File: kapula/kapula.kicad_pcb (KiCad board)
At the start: 4 copper layers, 50 x 59 mm, 167 parts, among them J1 Conn_02x10_Odd_Even, J12 U.FL, J13 U.FL, J3 Conn_02x10_Odd_Even, J4 Conn_ARM_JTAG_SWD_10, J5 U.FL, J9 U.FL, Q1 AO3401A, Q2 AO3401A, Q3 AO3400A, Q4 BSS84, Q5 AO3400A, Q6 AO3400A, T1 BW21S7511A01TF, T2 BW21S7511A01TF, T3 BW21S7511A01TF, T4 BW21S7511A01TF, U1 XC6206P332MR, U2 TP4054, U3 DW01+G, U5 EFR32FG14P233F256GM48-B, U6 XA213-G4J, X1 DSB221SDN, Y1 32768 Hz

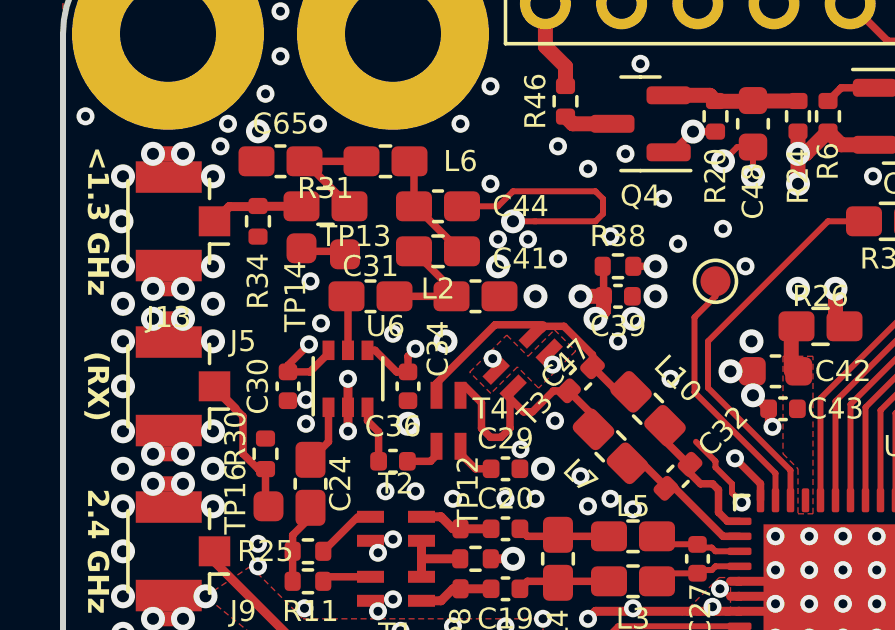
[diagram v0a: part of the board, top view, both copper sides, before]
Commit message: PCB: Improve RF layout
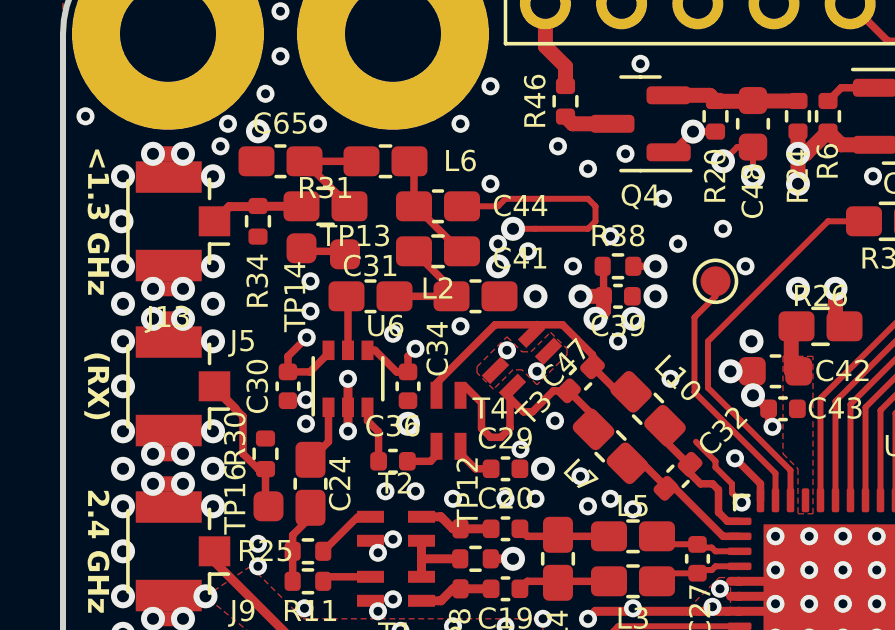
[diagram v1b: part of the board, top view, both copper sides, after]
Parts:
- moved NT2 0.25 mm to (115.5, 67.5)
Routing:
- net Net-(C44-Pad2): track 7.91 -> 7.31 mm

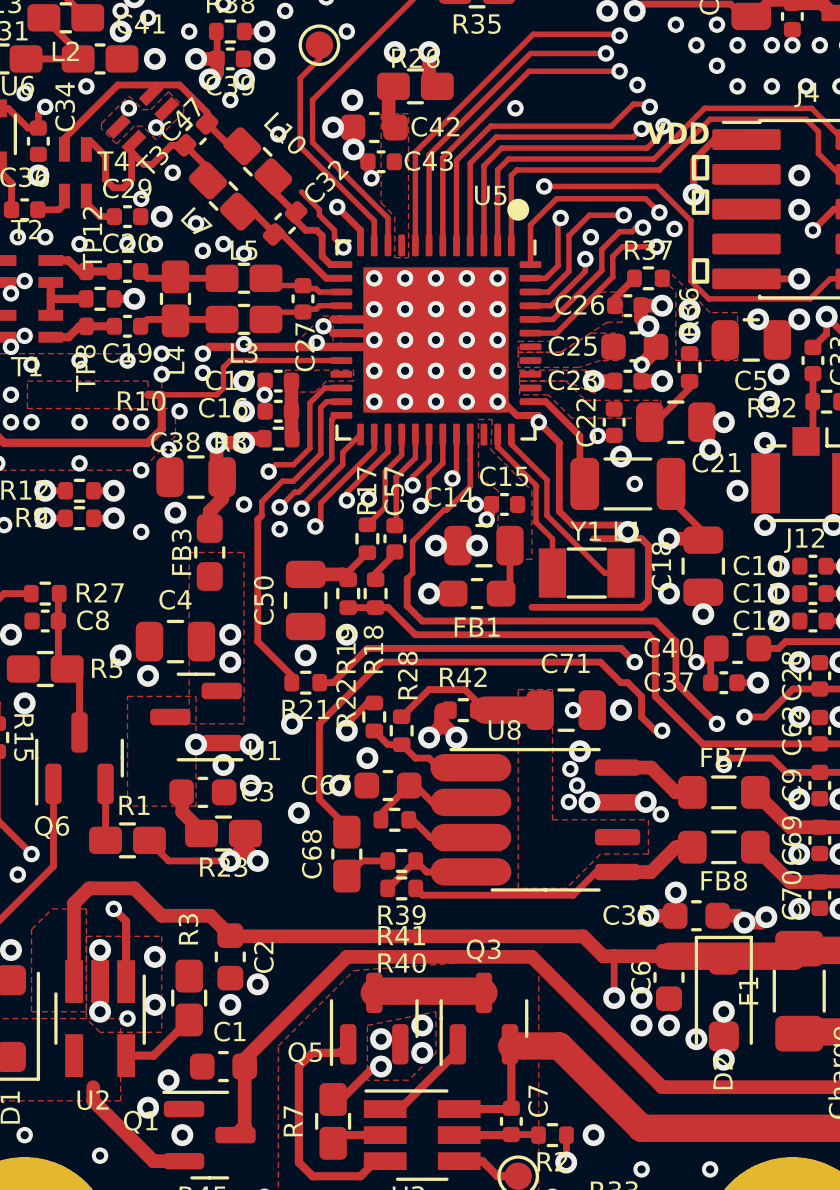
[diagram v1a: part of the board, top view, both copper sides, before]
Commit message: PCB: Make some planes and fills more continuous
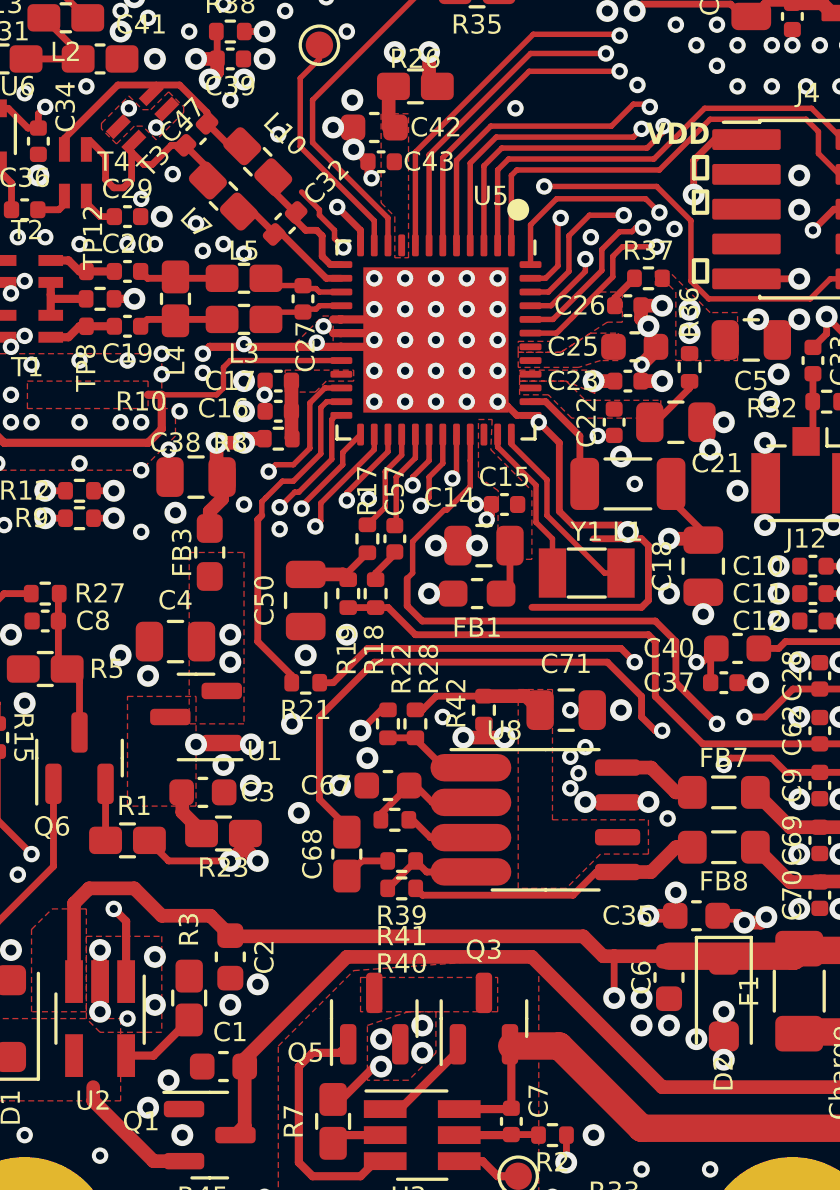
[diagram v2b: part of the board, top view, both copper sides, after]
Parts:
- moved R42 0.75 mm to (127.8, 93.5), turned to 90 degrees
- moved R22 0.56 mm to (124.2, 94.0)
- moved R28 0.56 mm to (125.2, 94.0)
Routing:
- net /BP_MID: track 4.05 -> 0.00 mm
- net GND: track 72.3 -> 71.3 mm, vias 388 -> 389
- net /VBAT: track 10.1 -> 9.17 mm
- net /AMP_VDD: track 5.77 -> 4.97 mm
- net /SPK_SDN: track 61.3 -> 60.6 mm
- added copper zone on F.Cu, net /BP_MID

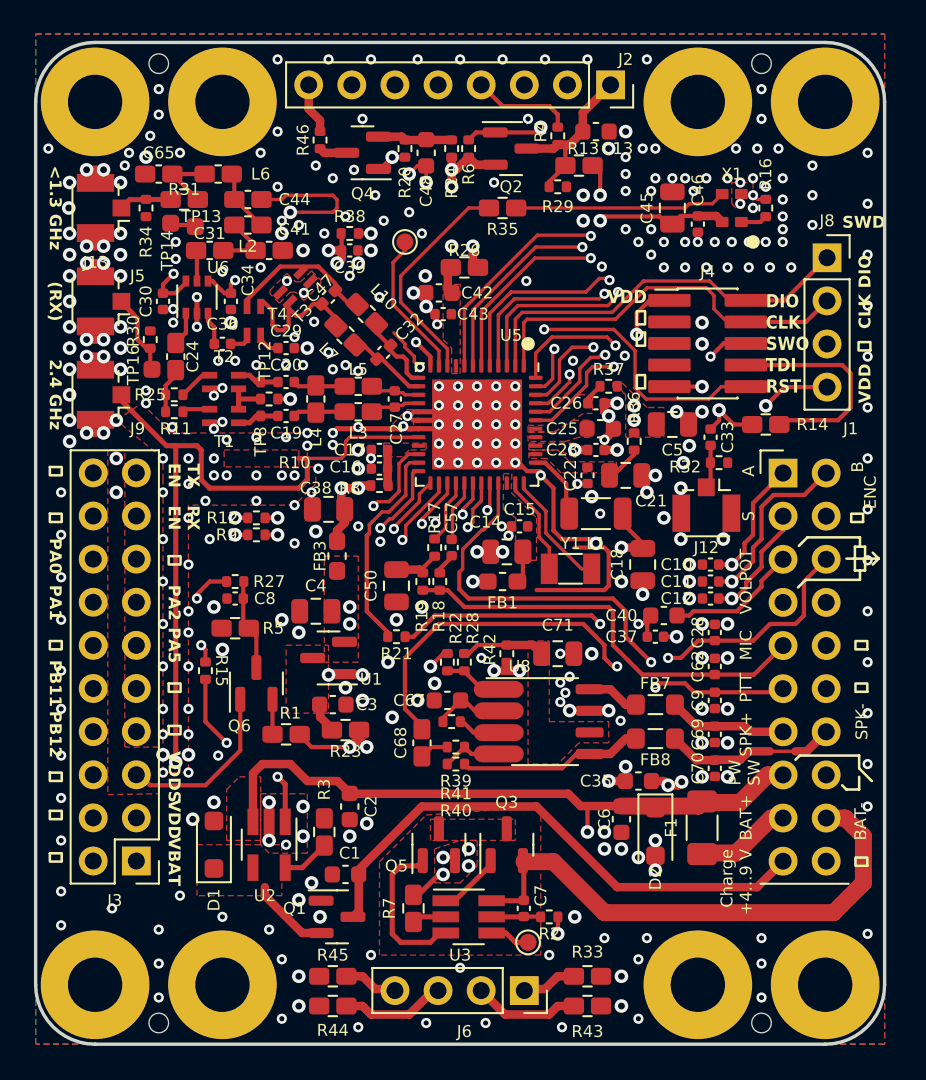
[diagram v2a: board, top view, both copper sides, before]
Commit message: PCB: Change some components, fix some DRC issues
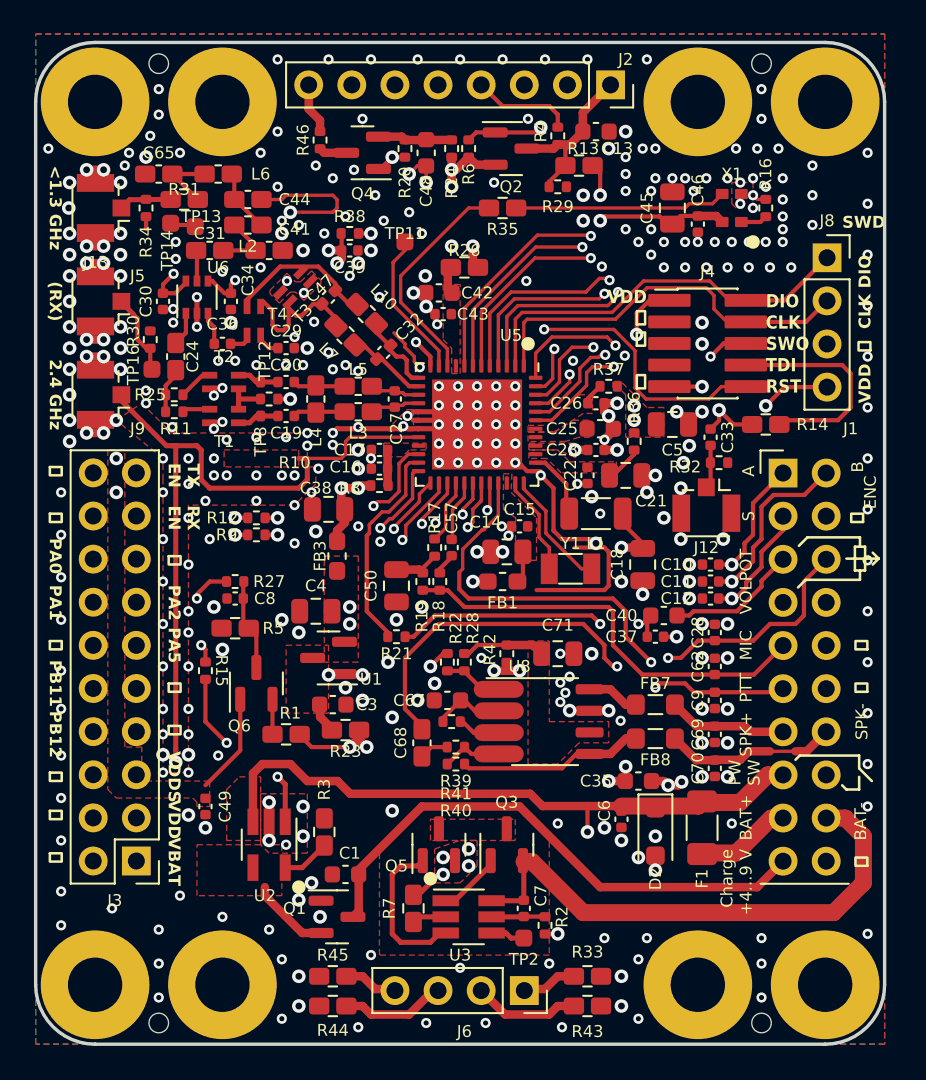
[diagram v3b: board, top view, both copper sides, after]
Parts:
- removed C2: 1u, Capacitor_SMD:C_0603_1608Metric
- removed D1: SM4007PL, Diode_SMD:D_SOD-123F
- added C49: 220n, Capacitor_SMD:C_0402_1005Metric, F.Cu at (110.0, 102.5)
- C6: value 1u -> 220n; footprint Capacitor_SMD:C_0603_1608Metric -> Capacitor_SMD:C_0402_1005Metric
- TP11, TP2: footprint TestPoint:TestPoint_Pad_D1.0mm -> kapula:Pad_1mm
- moved R2 0.56 mm to (130.0, 109.5), turned to 90 degrees
- moved TP2 0.35 mm to (128.8, 110.2)
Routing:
- net /VDDS: track 20.6 -> 16.4 mm
- net GND: track 71.3 -> 70.2 mm, vias 389 -> 388

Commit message: PCB: Move some vias away from pads a bit
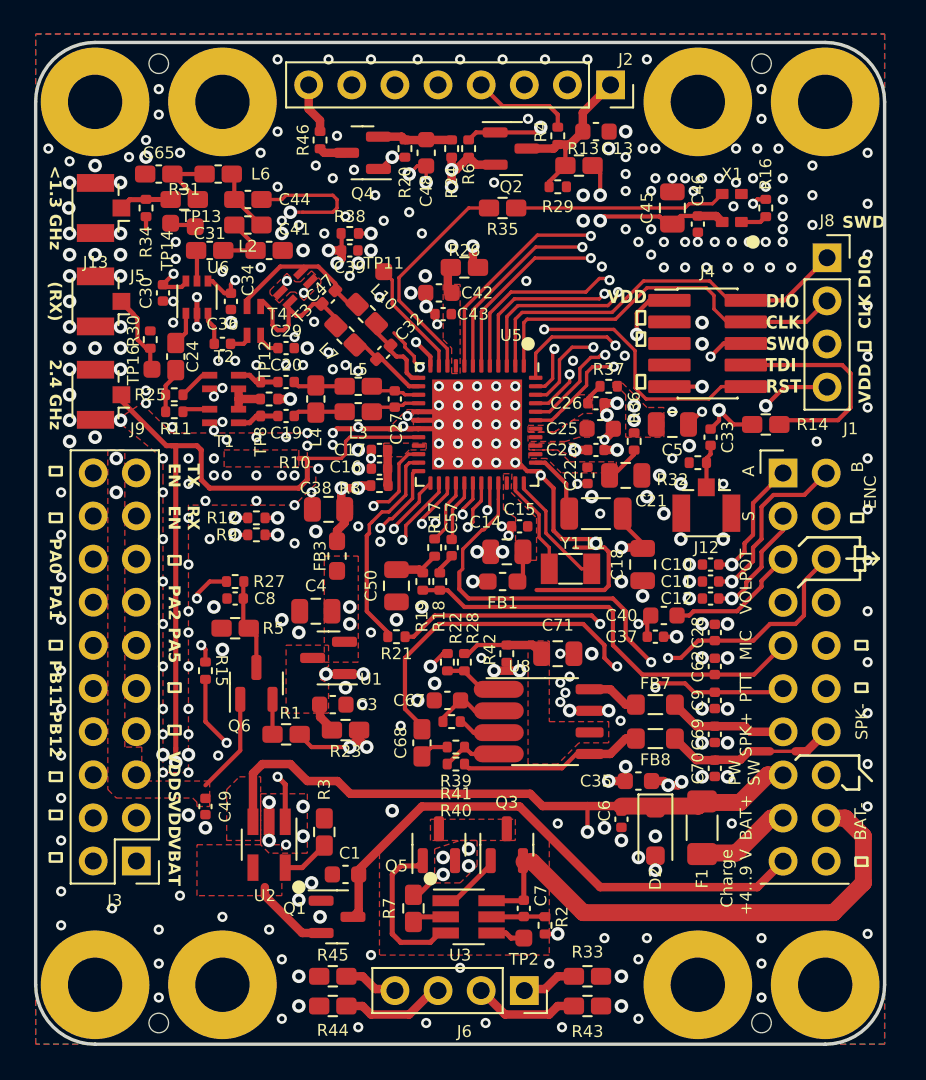
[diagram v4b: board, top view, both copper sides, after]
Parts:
- moved TP11 2.15 mm to (120.5, 71.0)
- moved R32 1.25 mm to (139.0, 82.2), turned to 0 degrees
- moved C30 0.50 mm to (107.5, 72.2)
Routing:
- net GND: track 70.2 -> 65.6 mm, vias 388 -> 381
- net /HFXTAL_P: track 8.71 -> 6.90 mm
- net /RX_EN_SW: track 21.6 -> 21.0 mm

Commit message: PCB: Move some silkscreen markings
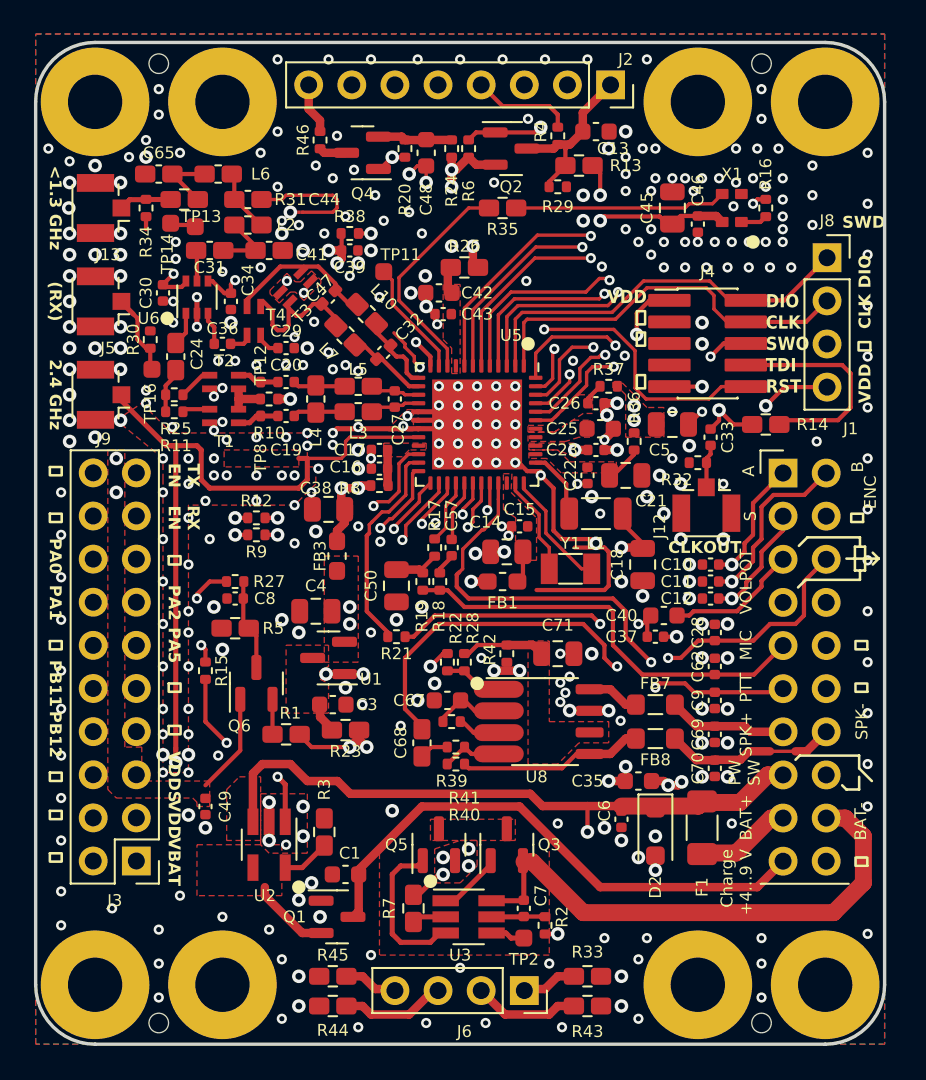
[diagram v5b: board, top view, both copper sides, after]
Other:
- board text added: "CLKOUT"

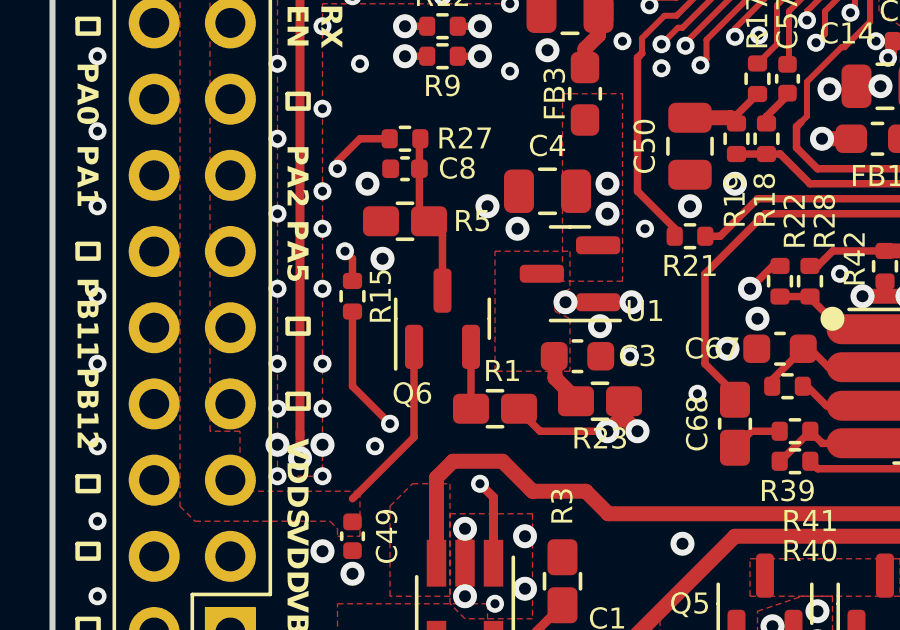
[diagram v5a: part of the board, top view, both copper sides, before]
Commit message: PCB: Fix bug in VBAT_ADC circuit
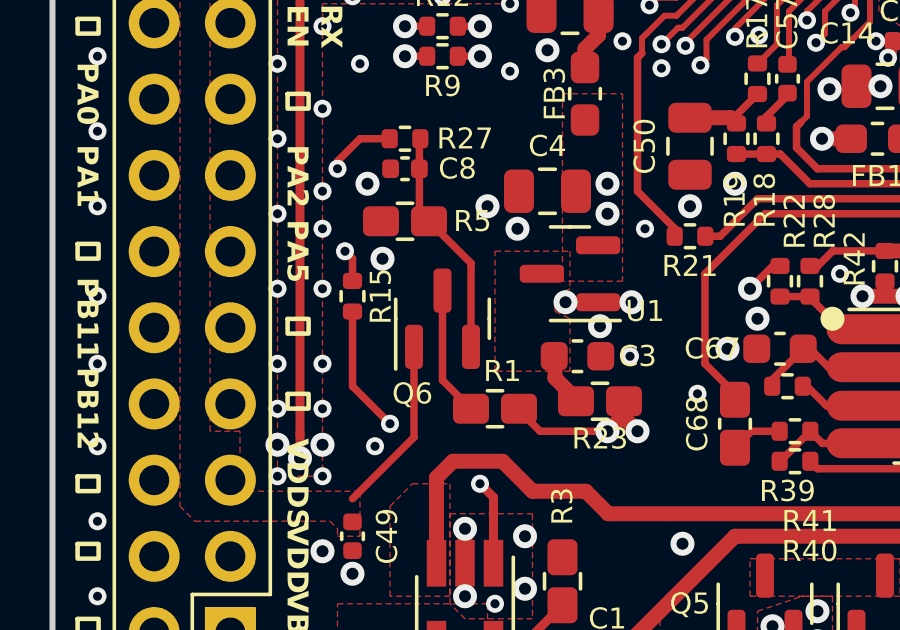
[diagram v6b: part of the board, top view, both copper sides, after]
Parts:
- J4: value Conn_ARM_JTAG_SWD_10 -> ~
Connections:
- Q6 pad 2: Net-(Q6-S) -> /VBAT_ADC
- Q6 pad 3: /VBAT_ADC -> Net-(Q6-D)
- R1 pad 1: Net-(Q6-S) -> Net-(Q6-D)
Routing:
- net Net-(Q6-D): track 0.00 -> 4.33 mm
- net /VBAT_ADC: track 5.39 -> 7.66 mm
- net Net-(Q6-S): track 2.06 -> 0.00 mm
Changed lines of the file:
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@@
   (net 105 "/SPK_SDN")
   (net 106 "/~{D_LED_EN}")
-  (net 107 "Net-(Q6-S)")
+  (net 107 "Net-(Q6-D)")
   (net 108 "/FILT_BYPASS")
   (net 109 "unconnected-(J4-KEY-Pad7)")
@@
       (stroke (width 0.1) (type solid)) (layer "F.Fab"))
     (pad "1" smd roundrect (at -0.8 0) (size 1.2 1) (layers "F.Cu" "F.Paste" "F.Mask") (roundrect_rratio 0.2)
-      (net 107 "Net-(Q6-S)") (pintype "passive"))
+      (net 107 "Net-(Q6-D)") (pintype "passive"))
     (pad "2" smd roundrect (at 0.8 0) (size 1.2 1) (layers "F.Cu" "F.Paste" "F.Mask") (roundrect_rratio 0.2)
       (net 34 "/VBAT") (pintype "passive"))
@@
         (effects (font (size 0.7 0.7) (thickness 0.15)))
     )
-    (fp_text value "Conn_ARM_JTAG_SWD_10" (at 0 4.235) (layer "F.Fab")
+    (fp_text value "~" (at 0 4.235) (layer "F.Fab")
         (effects (font (size 1 1) (thickness 0.15)))
     )
@@
       (net 33 "/VDDS") (pinfunction "G") (pintype "input"))
     (pad "2" smd roundrect (at -0.9375 0.95 90) (size 1.475 0.6) (layers "F.Cu" "F.Paste" "F.Mask") (roundrect_rratio 0.25)
-      (net 107 "Net-(Q6-S)") (pinfunction "S") (pintype "passive"))
+      (net 59 "/VBAT_ADC") (pinfunction "S") (pintype "passive"))
     (pad "3" smd roundrect (at 0.9375 0 90) (size 1.475 0.6) (layers "F.Cu" "F.Paste" "F.Mask") (roundrect_rratio 0.25)
-      (net 59 "/VBAT_ADC") (pinfunction "D") (pintype "passive"))
+      (net 107 "Net-(Q6-D)") (pinfunction "D") (pintype "passive"))
     (model "${KICAD6_3DMODEL_DIR}/Package_TO_SOT_SMD.3dshapes/SOT-23.wrl"
       (offset (xyz 0 0 0))
@@
   (segment (start 113 79.5) (end 113.25 79.5) (width 0.3) (layer "F.Cu") (net 58))
   (segment (start 114.27 79.5) (end 113.25 79.5) (width 0.3) (layer "F.Cu") (net 58))
-  (segment (start 113 94.3125) (end 113 92.45) (width 0.25) (layer "F.Cu") (net 59))
   (segment (start 112.23 90.25) (end 112.23 89.28) (width 0.25) (layer "F.Cu") (net 59))
-  (segment (start 113 92.45) (end 112.55 92) (width 0.25) (layer "F.Cu") (net 59))
   (segment (start 112.23 90.25) (end 112.23 91.68) (width 0.25) (layer "F.Cu") (net 59))
   (segment (start 112.23 89.28) (end 112.26 89.25) (width 0.25) (layer "F.Cu") (net 59))
   (segment (start 112.23 91.68) (end 112.55 92) (width 0.25) (layer "F.Cu") (net 59))
+  (segment (start 113.95 93.4) (end 112.55 92) (width 0.25) (layer "F.Cu") (net 59))
+  (segment (start 113.95 96.1875) (end 113.95 93.4) (width 0.25) (layer "F.Cu") (net 59))
   (segment (start 124.275 70.925) (end 124.45 70.75) (width 0.5) (layer "F.Cu") (net 60))
   (segment (start 124.275 72.25) (end 124.275 70.925) (width 0.5) (layer "F.Cu") (net 60))
@@
   (segment (start 130.425 72.125) (end 130.425 73.925) (width 0.25) (layer "In2.Cu") (net 106))
   (segment (start 130.75 74.25) (end 130.75 75.35) (width 0.25) (layer "In2.Cu") (net 106))
-  (segment (start 113.95 96.1875) (end 113.95 98.25) (width 0.25) (layer "F.Cu") (net 107))
+  (segment (start 113 94.3125) (end 113 97.3) (width 0.25) (layer "F.Cu") (net 107))
+  (segment (start 113 97.3) (end 113.95 98.25) (width 0.25) (layer "F.Cu") (net 107))
   (segment (start 107.975 68.25) (end 109.225 68.25) (width 0.25) (layer "F.Cu") (net 108))
   (segment (start 147.25 79.75) (end 144.05 79.75) (width 0.25) (layer "F.Cu") (net 110))
